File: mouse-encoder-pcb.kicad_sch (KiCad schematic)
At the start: 9 parts, among them SW1 RotaryEncoder, U2 FPC_0_5-8P_HYH2_0

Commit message: working square version
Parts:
- removed U2: FPC_0_5-8P_HYH2_0, MyKicadFootprints:FPC-SMD_8P-P0.50_AFC24-S08FCA-00, symbol MyKicadSymbols:FPC_0_5-8P_HYH2_0
- added J1: vik-module-connector, MyKicadFootprints:FPC-SMD_12P-P0.50_HCTL_XW05202-120R-00, symbol Vik:vik-module-connector
- added LOGO2: **REF, Vik:vik-logo-small, symbol MyKicadSymbols:awesome-logo
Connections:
- net +3V3: now also J1.12 (3V3)
- net GND: now also J1.11 (GND)
- net at C2.1, R3.1: now also J1.6 (GP_AD1)
- net at C1.1, R4.1: now also J1.4 (GP_AD2)
- no-connect marks 0 -> 8

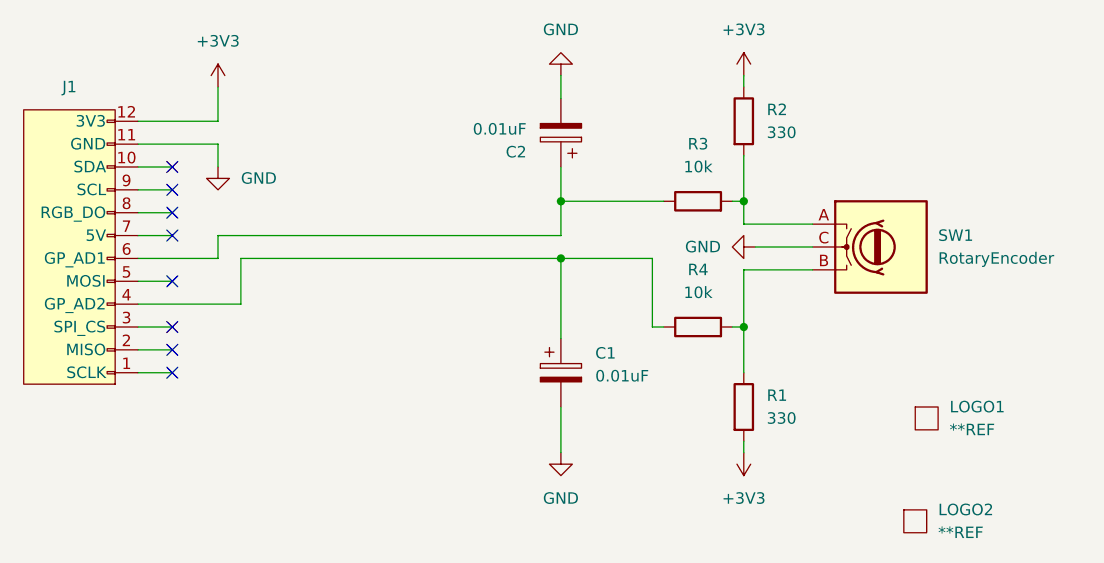
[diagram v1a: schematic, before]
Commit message: updating footprints
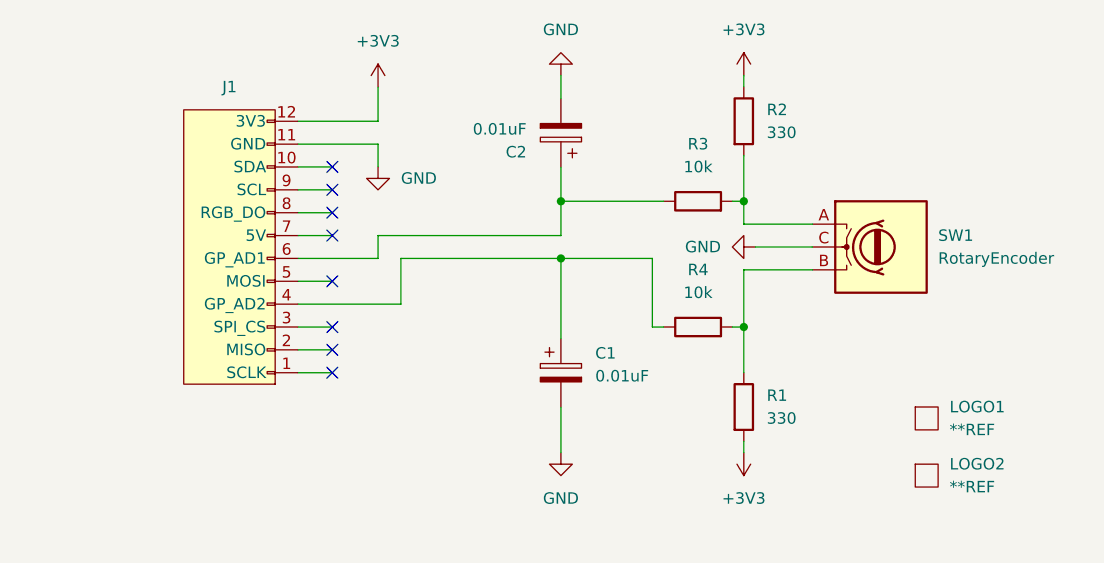
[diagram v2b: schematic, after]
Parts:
- J1: footprint MyKicadFootprints:FPC-SMD_12P-P0.50_HCTL_XW05202-120R-00 -> MyKicadFootprints:FFC-SMD_FFC05001-12SBA124W5M
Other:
- moved on the sheet: J1, LOGO2
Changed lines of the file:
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@@
 	)
 	(no_connect
-		(at 69.85 80.01)
+		(at 87.63 80.01)
 	)
 	(no_connect
-		(at 69.85 90.17)
+		(at 87.63 90.17)
 	)
 	(no_connect
-		(at 69.85 67.31)
+		(at 87.63 67.31)
 	)
 	(no_connect
-		(at 69.85 87.63)
+		(at 87.63 87.63)
 	)
 	(no_connect
-		(at 69.85 69.85)
+		(at 87.63 69.85)
 	)
 	(no_connect
-		(at 69.85 72.39)
+		(at 87.63 72.39)
 	)
 	(no_connect
-		(at 69.85 85.09)
+		(at 87.63 85.09)
 	)
 	(no_connect
-		(at 69.85 74.93)
+		(at 87.63 74.93)
 	)
 	(wire
@@
 	(wire
 		(pts
-			(xy 74.93 74.93) (xy 74.93 77.47)
+			(xy 92.71 74.93) (xy 92.71 77.47)
 		)
 		(stroke
@@
 	(wire
 		(pts
-			(xy 77.47 77.47) (xy 113.03 77.47)
-		)
-		(stroke
-			(width 0)
-			(type default)
-		)
-	)
-	(wire
-		(pts
-			(xy 74.93 77.47) (xy 66.04 77.47)
-		)
-		(stroke
-			(width 0)
-			(type default)
-		)
-	)
-	(wire
-		(pts
-			(xy 77.47 77.47) (xy 77.47 82.55)
+			(xy 95.25 77.47) (xy 113.03 77.47)
+		)
+		(stroke
+			(width 0)
+			(type default)
+		)
+	)
+	(wire
+		(pts
+			(xy 92.71 77.47) (xy 83.82 77.47)
+		)
+		(stroke
+			(width 0)
+			(type default)
+		)
+	)
+	(wire
+		(pts
+			(xy 95.25 77.47) (xy 95.25 82.55)
 		)
 		(stroke
@@
 	(wire
 		(pts
-			(xy 74.93 64.77) (xy 74.93 67.31)
+			(xy 92.71 64.77) (xy 92.71 67.31)
 		)
 		(stroke
@@
 	(wire
 		(pts
-			(xy 66.04 74.93) (xy 69.85 74.93)
+			(xy 83.82 74.93) (xy 87.63 74.93)
 		)
 		(stroke
@@
 	(wire
 		(pts
-			(xy 66.04 64.77) (xy 74.93 64.77)
+			(xy 83.82 64.77) (xy 92.71 64.77)
 		)
 		(stroke
@@
 	(wire
 		(pts
-			(xy 66.04 67.31) (xy 69.85 67.31)
-		)
-		(stroke
-			(width 0)
-			(type default)
-		)
-	)
-	(wire
-		(pts
-			(xy 66.04 69.85) (xy 69.85 69.85)
+			(xy 83.82 67.31) (xy 87.63 67.31)
+		)
+		(stroke
+			(width 0)
+			(type default)
+		)
+	)
+	(wire
+		(pts
+			(xy 83.82 69.85) (xy 87.63 69.85)
 		)
 		(stroke
@@
 	(wire
 		(pts
-			(xy 77.47 82.55) (xy 66.04 82.55)
+			(xy 95.25 82.55) (xy 83.82 82.55)
 		)
 		(stroke
@@
 	(wire
 		(pts
-			(xy 66.04 85.09) (xy 69.85 85.09)
-		)
-		(stroke
-			(width 0)
-			(type default)
-		)
-	)
-	(wire
-		(pts
-			(xy 74.93 62.23) (xy 66.04 62.23)
-		)
-		(stroke
-			(width 0)
-			(type default)
-		)
-	)
-	(wire
-		(pts
-			(xy 66.04 72.39) (xy 69.85 72.39)
-		)
-		(stroke
-			(width 0)
-			(type default)
-		)
-	)
-	(wire
-		(pts
-			(xy 66.04 87.63) (xy 69.85 87.63)
+			(xy 83.82 85.09) (xy 87.63 85.09)
+		)
+		(stroke
+			(width 0)
+			(type default)
+		)
+	)
+	(wire
+		(pts
+			(xy 92.71 62.23) (xy 83.82 62.23)
+		)
+		(stroke
+			(width 0)
+			(type default)
+		)
+	)
+	(wire
+		(pts
+			(xy 83.82 72.39) (xy 87.63 72.39)
+		)
+		(stroke
+			(width 0)
+			(type default)
+		)
+	)
+	(wire
+		(pts
+			(xy 83.82 87.63) (xy 87.63 87.63)
 		)
 		(stroke
@@
 	(wire
 		(pts
-			(xy 66.04 90.17) (xy 69.85 90.17)
-		)
-		(stroke
-			(width 0)
-			(type default)
-		)
-	)
-	(wire
-		(pts
-			(xy 74.93 58.42) (xy 74.93 62.23)
+			(xy 83.82 90.17) (xy 87.63 90.17)
+		)
+		(stroke
+			(width 0)
+			(type default)
+		)
+	)
+	(wire
+		(pts
+			(xy 92.71 58.42) (xy 92.71 62.23)
 		)
 		(stroke
@@
 	(wire
 		(pts
-			(xy 74.93 74.93) (xy 113.03 74.93)
-		)
-		(stroke
-			(width 0)
-			(type default)
-		)
-	)
-	(wire
-		(pts
-			(xy 66.04 80.01) (xy 69.85 80.01)
+			(xy 92.71 74.93) (xy 113.03 74.93)
+		)
+		(stroke
+			(width 0)
+			(type default)
+		)
+	)
+	(wire
+		(pts
+			(xy 83.82 80.01) (xy 87.63 80.01)
 		)
 		(stroke
@@
 	(symbol
 		(lib_id "MyKicadSymbols:awesome-logo")
-		(at 152.4 106.68 0)
+		(at 153.67 101.6 0)
 		(unit 1)
 		(exclude_from_sim no)
@@
 		(fields_autoplaced yes)
 		(property "Reference" "LOGO2"
-			(at 154.94 105.4099 0)
+			(at 156.21 100.3299 0)
 			(effects
 				(font
@@
 		)
 		(property "Value" "**REF"
-			(at 154.94 107.9499 0)
+			(at 156.21 102.8699 0)
 			(effects
 				(font
@@
 		)
 		(property "Footprint" "Vik:vik-logo-small"
-			(at 152.4 106.68 0)
+			(at 153.67 101.6 0)
 			(effects
 				(font
@@
 		)
 		(property "Datasheet" ""
-			(at 152.4 106.68 0)
+			(at 153.67 101.6 0)
 			(effects
 				(font
@@
 		)
 		(property "Description" "the crazymittens logo"
-			(at 152.4 106.68 0)
+			(at 153.67 101.6 0)
 			(effects
 				(font
@@
 	(symbol
 		(lib_id "Vik:vik-module-connector")
-		(at 58.42 77.47 180)
+		(at 76.2 77.47 180)
 		(unit 1)
 		(exclude_from_sim no)
@@
 		(fields_autoplaced yes)
 		(property "Reference" "J1"
-			(at 58.4323 58.42 0)
+			(at 76.2123 58.42 0)
 			(effects
 				(font
@@
 		)
 		(property "Value" "vik-module-connector"
-			(at 58.42 59.69 0)
-			(effects
-				(font
-					(size 1.27 1.27)
-				)
-				(hide yes)
-			)
-		)
-		(property "Footprint" "MyKicadFootprints:FPC-SMD_12P-P0.50_HCTL_XW05202-120R-00"
-			(at 58.42 83.82 0)
+			(at 76.2 59.69 0)
+			(effects
+				(font
+					(size 1.27 1.27)
+				)
+				(hide yes)
+			)
+		)
+		(property "Footprint" "MyKicadFootprints:FFC-SMD_FFC05001-12SBA124W5M"
+			(at 76.2 83.82 0)
 			(effects
 				(font
@@
 		)
 		(property "Datasheet" ""
-			(at 58.42 83.82 0)
+			(at 76.2 83.82 0)
 			(effects
 				(font
@@
 		)
 		(property "Description" ""
-			(at 58.42 77.47 0)
+			(at 76.2 77.47 0)
 			(effects
 				(font
@@
 	(symbol
 		(lib_id "power:GND")
-		(at 74.93 67.31 0)
+		(at 92.71 67.31 0)
 		(unit 1)
 		(exclude_from_sim no)
@@
 		(fields_autoplaced yes)
 		(property "Reference" "#PWR08"
-			(at 74.93 73.66 0)
+			(at 92.71 73.66 0)
 			(effects
 				(font
@@
 		)
 		(property "Value" "GND"
-			(at 77.47 68.5799 0)
+			(at 95.25 68.5799 0)
 			(effects
 				(font
@@
 		)
 		(property "Footprint" ""
-			(at 74.93 67.31 0)
+			(at 92.71 67.31 0)
 			(effects
 				(font
@@
 		)
 		(property "Datasheet" ""
-			(at 74.93 67.31 0)
+			(at 92.71 67.31 0)
 			(effects
 				(font
@@
 		)
 		(property "Description" "Power symbol creates a global label with name \"GND\" , ground"
-			(at 74.93 67.31 0)
+			(at 92.71 67.31 0)
 			(effects
 				(font
@@
 	(symbol
 		(lib_id "power:+3V3")
-		(at 74.93 58.42 0)
+		(at 92.71 58.42 0)
 		(unit 1)
 		(exclude_from_sim no)
@@
 		(fields_autoplaced yes)
 		(property "Reference" "#PWR07"
-			(at 74.93 62.23 0)
+			(at 92.71 62.23 0)
 			(effects
 				(font
@@
 		)
 		(property "Value" "+3V3"
-			(at 74.93 53.34 0)
+			(at 92.71 53.34 0)
 			(effects
 				(font
@@
 		)
 		(property "Footprint" ""
-			(at 74.93 58.42 0)
+			(at 92.71 58.42 0)
 			(effects
 				(font
@@
 		)
 		(property "Datasheet" ""
-			(at 74.93 58.42 0)
+			(at 92.71 58.42 0)
 			(effects
 				(font
@@
 		)
 		(property "Description" "Power symbol creates a global label with name \"+3V3\""
-			(at 74.93 58.42 0)
-			(effects
-				(font
+			(at 92.71 58.42 0)
+			(effects
+				(font
